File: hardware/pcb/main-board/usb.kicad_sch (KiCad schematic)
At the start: 51 parts, among them J6 xSYS2, J7 USB_C_Receptacle_USB2.0_16P, U16 74AHCT125, U17 W25Q32JVSS, U18 PTN5150AHXMP, U19 XU316-1024-TQ128-C24, Y1 TKC 7M 24MHz

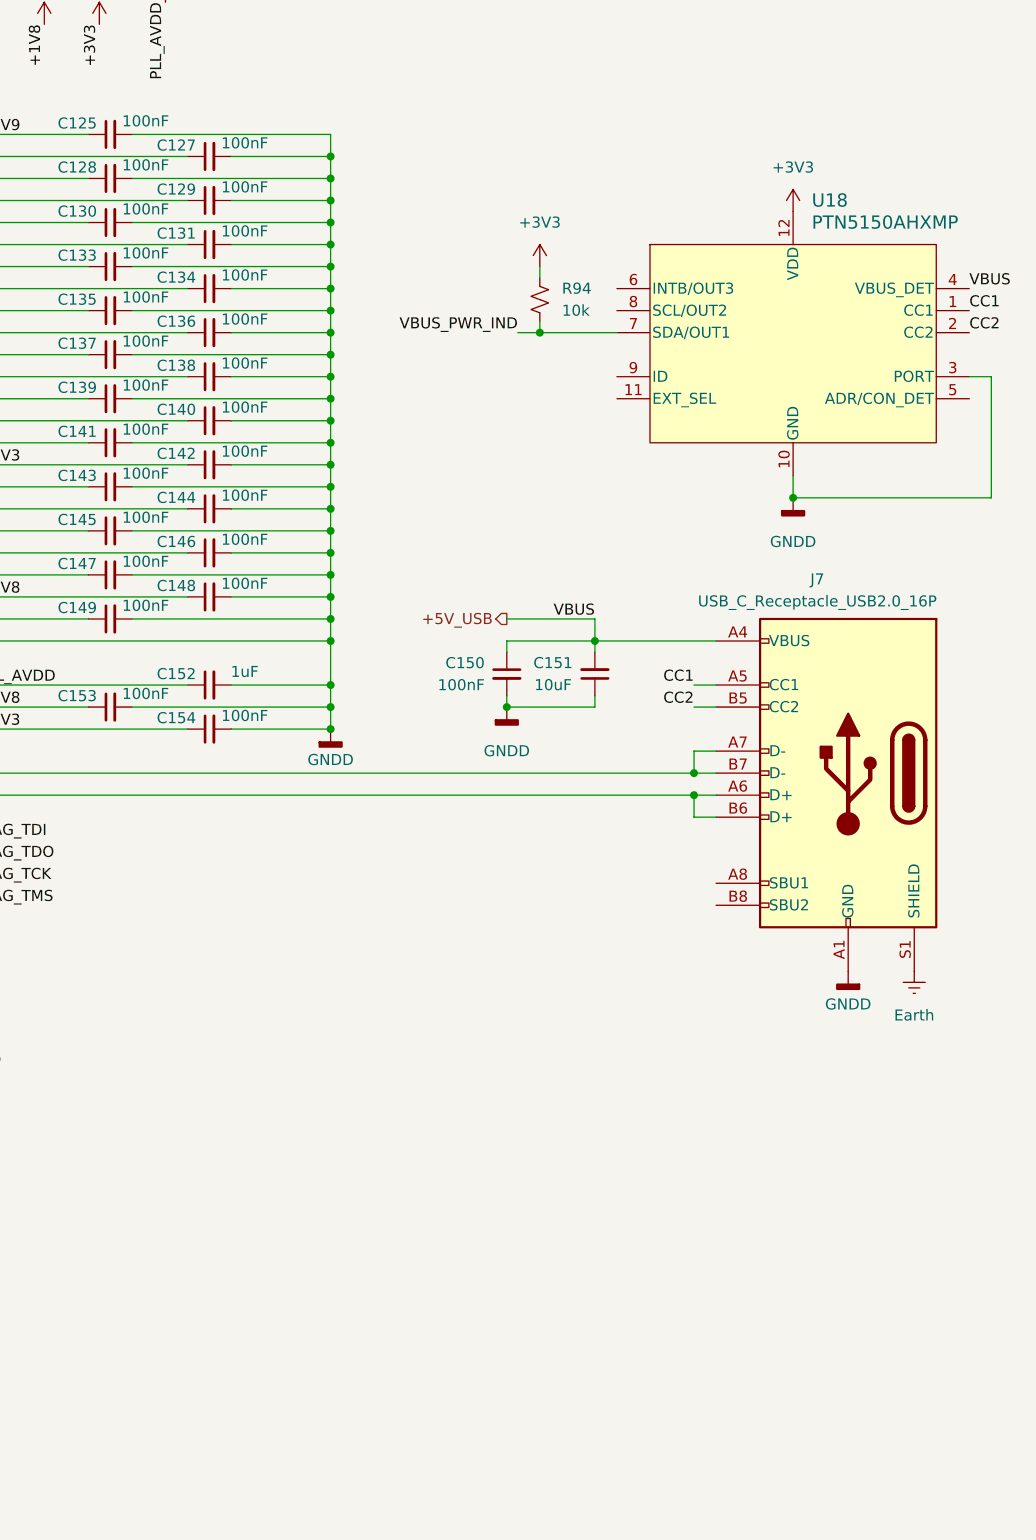
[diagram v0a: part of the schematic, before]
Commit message: update power supply to prototype circuit
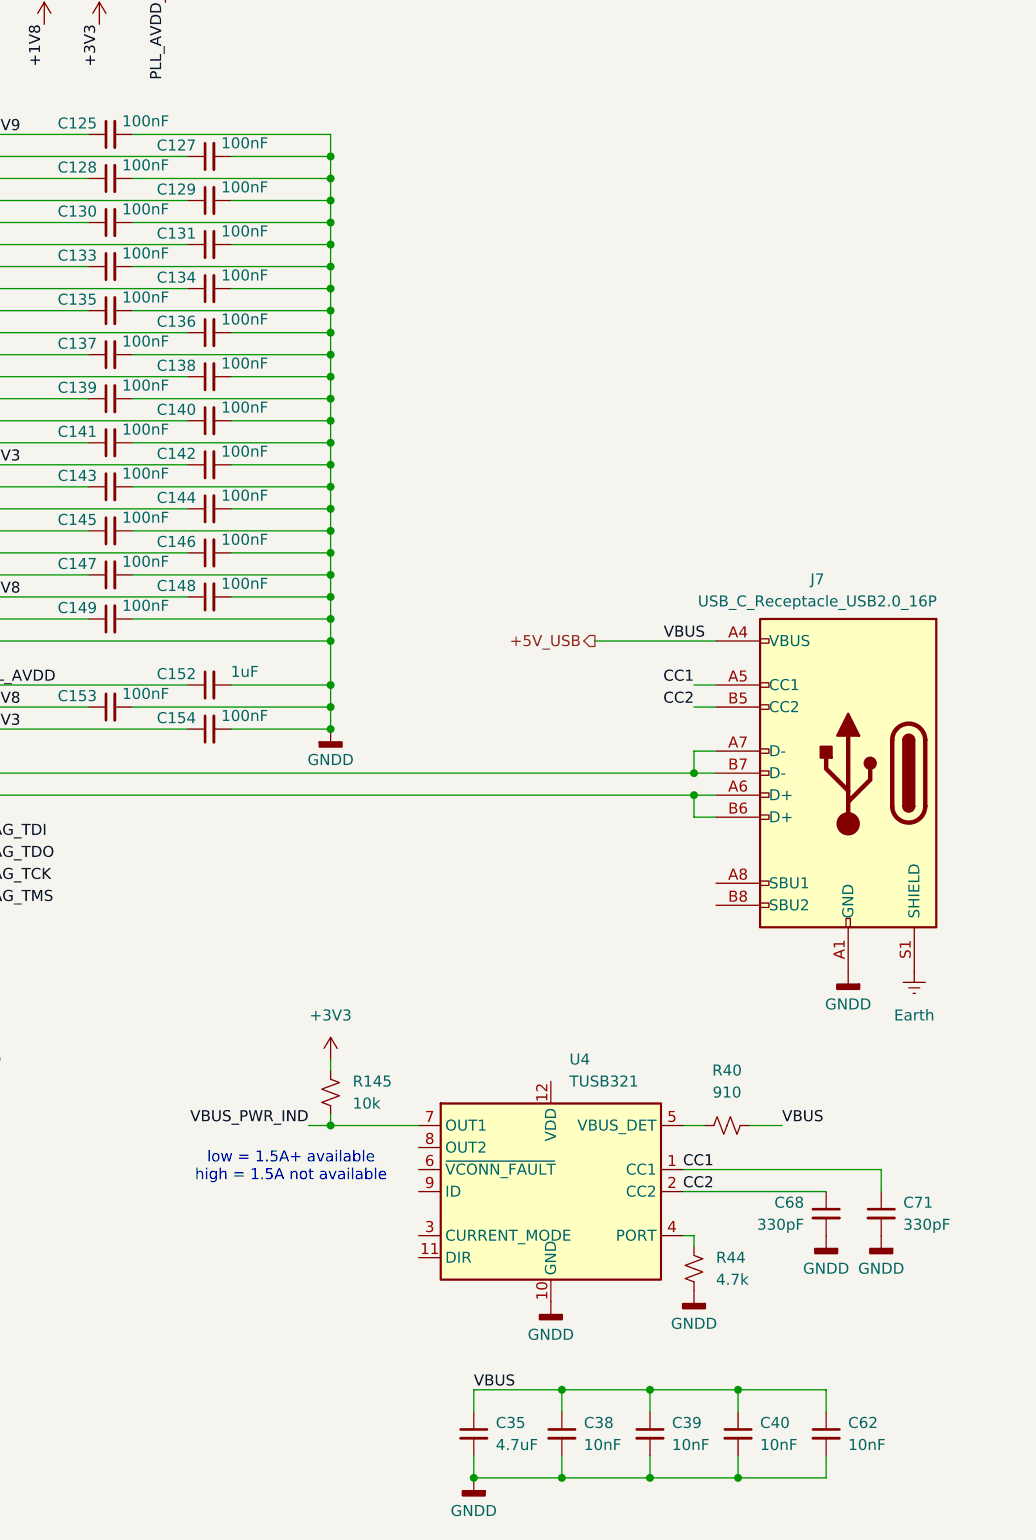
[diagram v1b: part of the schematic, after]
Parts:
- removed C150: 100nF, Capacitor_SMD:C_0805_2012Metric_Pad1.18x1.45mm_HandSolder, symbol Device:C_Small
- removed C151: 10uF, Capacitor_SMD:C_0805_2012Metric_Pad1.18x1.45mm_HandSolder, symbol Device:C_Small
- removed R94: 10k, Resistor_SMD:R_0603_1608Metric_Pad0.98x0.95mm_HandSolder, symbol Device:R_Small_US
- removed U18: PTN5150AHXMP, Package_DFN_QFN:Texas_X2QFN-12_1.6x1.6mm_P0.4mm, symbol openmic:PTN5150AHXMP
- added C35: 4.7uF, Capacitor_SMD:C_0805_2012Metric_Pad1.18x1.45mm_HandSolder, symbol Device:C_Small
- added C38, C39, C40, C62: 10nF, Capacitor_SMD:C_0805_2012Metric_Pad1.18x1.45mm_HandSolder, symbol Device:C_Small
- added C68, C71: 330pF, Capacitor_SMD:C_0805_2012Metric_Pad1.18x1.45mm_HandSolder, symbol Device:C_Small
- added R145: 10k, Resistor_SMD:R_0603_1608Metric_Pad0.98x0.95mm_HandSolder, symbol Device:R_Small_US
- added R40: 910, Resistor_SMD:R_0805_2012Metric_Pad1.20x1.40mm_HandSolder, symbol Device:R_Small_US
- added R44: 4.7k, Resistor_SMD:R_0805_2012Metric_Pad1.20x1.40mm_HandSolder, symbol Device:R_Small_US
- added U4: TUSB321, Package_DFN_QFN:Texas_X2QFN-12_1.6x1.6mm_P0.4mm, symbol Interface_USB:TUSB321
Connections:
- net +3V3: now also R145.1
- net +5V_USB: now also C35.1, C38.1, C39.1, C40.1, C62.1, R40.2
- net CC1: now also C71.1, U4.1 (CC1)
- net CC2: now also C68.1, U4.2 (CC2)
- net GNDD: now also C35.2, C38.2, C39.2, C40.2, C62.2, C68.2, C71.2, R44.1, U4.10 (GND)
- net GP0_8D_0: now also R145.2, U4.7 (OUT1)
- new net: R44.2, U4.4 (PORT)
- new net: R40.1, U4.5 (VBUS_DET)
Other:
- note added: "low = 1.5A+ available high = 1.5A not available"

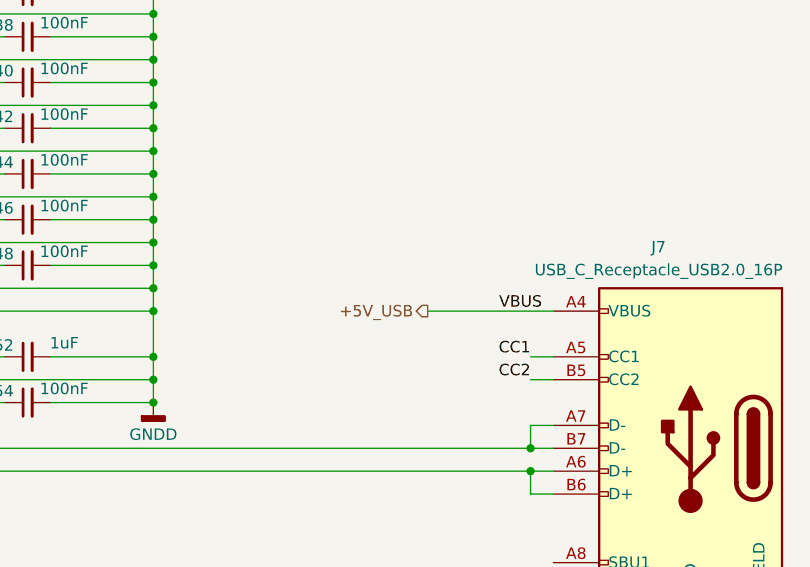
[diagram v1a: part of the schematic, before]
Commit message: add ptc fuses to phantom and usb supplies
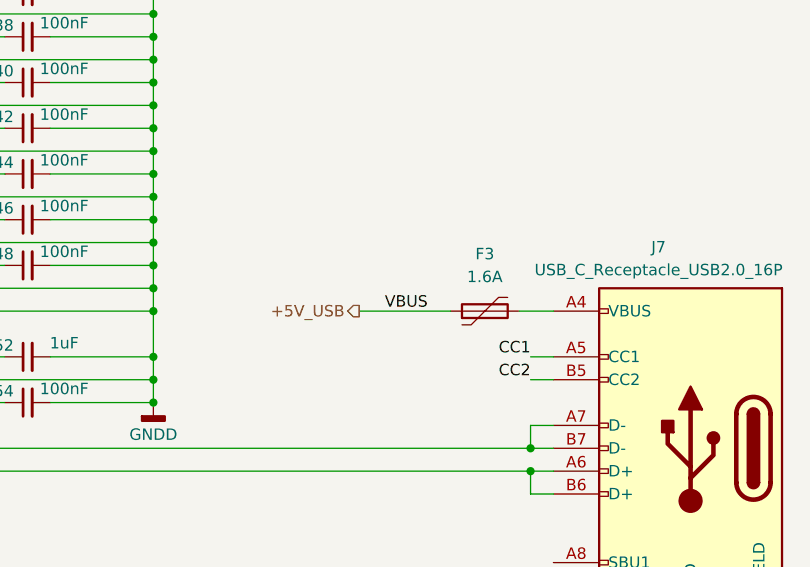
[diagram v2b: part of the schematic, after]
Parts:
- added F3: 1.6A, symbol Device:Polyfuse
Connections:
- net +5V_USB: now also F3.1; no longer J7.A4 (VBUS), J7.A9 (VBUS), J7.B4 (VBUS), J7.B9 (VBUS)
- new net: F3.2, J7.A4 (VBUS), J7.A9 (VBUS), J7.B4 (VBUS), J7.B9 (VBUS)
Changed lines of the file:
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@@
 	(wire
 		(pts
+			(xy 374.65 124.46) (xy 378.46 124.46)
+		)
+		(stroke
+			(width 0)
+			(type default)
+		)
+	)
+	(wire
+		(pts
 			(xy 34.29 95.25) (xy 34.29 92.71)
 		)
@@
 	(wire
 		(pts
-			(xy 364.49 124.46) (xy 378.46 124.46)
+			(xy 356.87 124.46) (xy 367.03 124.46)
 		)
 		(stroke
@@
 	)
 	(label "VBUS"
-		(at 377.19 124.46 180)
+		(at 364.49 124.46 180)
 		(effects
 			(font
@@
 	(hierarchical_label "+5V_USB"
 		(shape output)
-		(at 364.49 124.46 180)
+		(at 356.87 124.46 180)
 		(effects
 			(font
@@
 					(unit 1)
 				)
+			)
+		)
+	)
+	(symbol
+		(lib_id "Device:Polyfuse")
+		(at 370.84 124.46 90)
+		(unit 1)
+		(body_style 1)
+		(exclude_from_sim no)
+		(in_bom yes)
+		(on_board yes)
+		(in_pos_files yes)
+		(dnp no)
+		(fields_autoplaced yes)
+		(property "Reference" "F3"
+			(at 370.84 118.11 90)
+			(show_name no)
+			(do_not_autoplace no)
+			(effects
+				(font
+					(size 1.27 1.27)
+				)
+			)
+		)
+		(property "Value" "1.6A"
+			(at 370.84 120.65 90)
+			(show_name no)
+			(do_not_autoplace no)
+			(effects
+				(font
+					(size 1.27 1.27)
+				)
+			)
+		)
+		(property "Footprint" ""
+			(at 375.92 123.19 0)
+			(hide yes)
+			(show_name no)
+			(do_not_autoplace no)
+			(effects
+				(font
+					(size 1.27 1.27)
+				)
+				(justify left)
+			)
+		)
+		(property "Datasheet" ""
+			(at 370.84 124.46 0)
+			(hide yes)
+			(show_name no)
+			(do_not_autoplace no)
+			(effects
+				(font
+					(size 1.27 1.27)
+				)
+			)
+		)
+		(property "Description" "Resettable fuse, polymeric positive temperature coefficient"
+			(at 370.84 124.46 0)
+			(hide yes)
+			(show_name no)
+			(do_not_autoplace no)
+			(effects
+				(font
+					(size 1.27 1.27)
+				)
+			)
+		)
+		(pin "2"
+		)
+		(pin "1"
+		)
+		(instances
+			(project "openmic"
+				(path "/84faeadc-8b12-4a66-a17f-5c56e5923fb8/ac4749a9-b66d-4a3a-8eaa-94f1fe3c6a5c"
+					(reference "F3")
+					(unit 1)
+				)
